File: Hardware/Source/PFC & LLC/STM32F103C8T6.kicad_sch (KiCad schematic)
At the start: 107 parts, among them J3 Conn_01x06_Socket, J4 Conn_01x02_Socket, J5 Conn_01x04_Pin, J6 Conn_01x05_Socket, Q6 LN2302LT1G, Q7 LN2302LT1G, Q8 LN2302LT1G, Q9 MMBT2222A, SW1 SW_Push, U10 ADS1115IDGS, U11 STM32F103C8T6, U12 MAX485CSA, Y1 Crystal_8MHz_SMD-4PIN

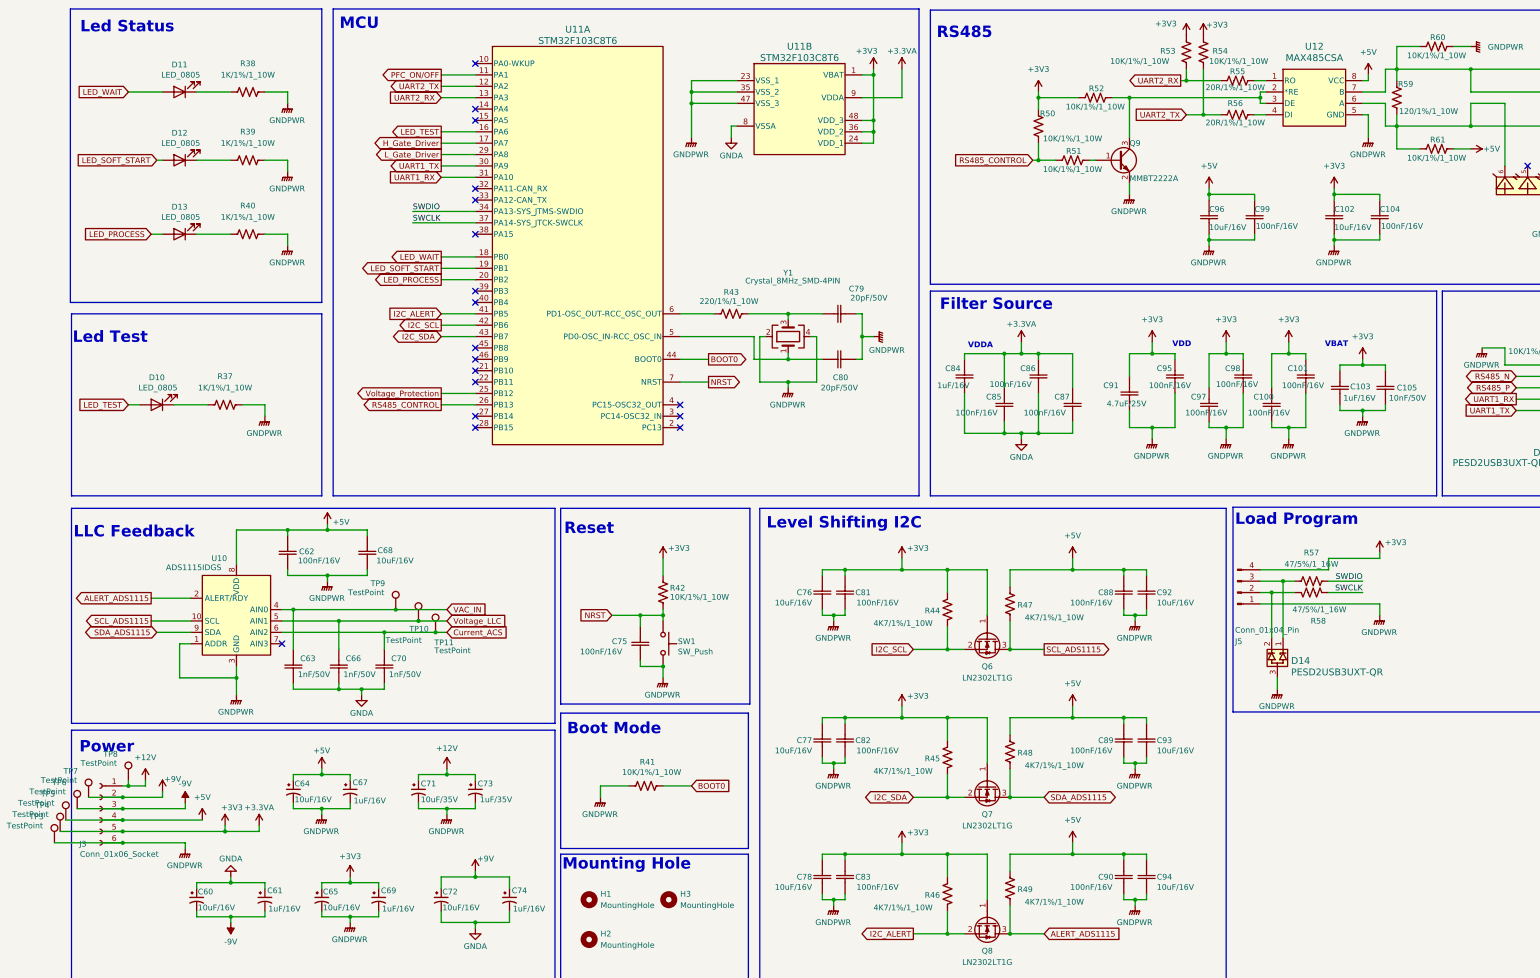
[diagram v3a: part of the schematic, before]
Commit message: Update PFC&LLC
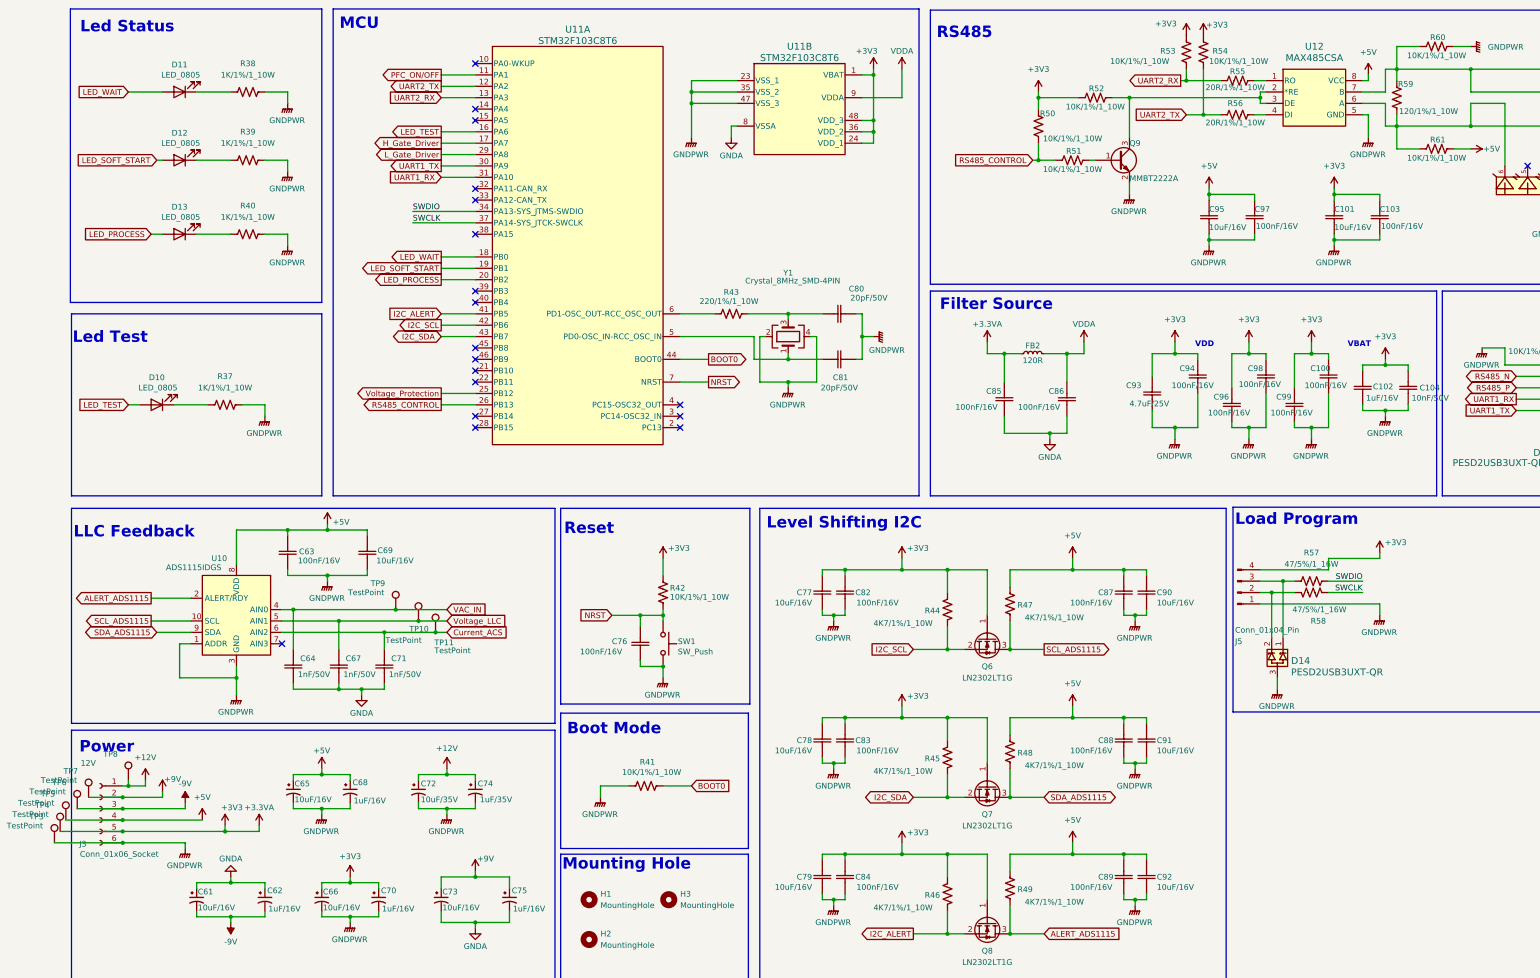
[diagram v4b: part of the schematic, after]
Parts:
- removed C84: 1uF/16V, charge_battery_footprint_lib:Ceramic_Cap_0603, symbol charge_battery_sym_lib:Ceramic_Cap_SMD_1uF_16V
- removed C87: 100nF/16V, charge_battery_footprint_lib:Ceramic_Cap_0603, symbol charge_battery_sym_lib:Ceramic_Cap_SMD_100nF_16V
- added FB2: 120R, Inductor_SMD:L_0805_2012Metric, symbol Device:L_Small
- TP8: value TestPoint -> 12V
- renumbered C101 to C100, C102 to C101, C103 to C102, C104 to C103, C105 to C104, C60 to C61, C61 to C62, C62 to C63, C63 to C64, C64 to C65, C65 to C66, C66 to C67, C67 to C68, C68 to C69, C69 to C70, C70 to C71, C71 to C72, C72 to C73, C73 to C74, C74 to C75, C75 to C76, C76 to C77, C77 to C78, C78 to C79, C79 to C80, C80 to C81, C81 to C82, C82 to C83, C83 to C84, C88 to C87, C89 to C88, C90 to C89, C92 to C90, C93 to C91, C94 to C92, C91 to C93, C95 to C94, C96 to C95, C97 to C96, C99 to C97, C100 to C99
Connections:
- net +3.3VA: now also FB2.1; no longer C86.2, U11.9 (VDDA)
- new net VDDA: C86.2, FB2.2, U11.9 (VDDA)
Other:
- note removed: "VDDA"
- moved on the sheet: C100, C102, C104, C85, C86, C93, C94, C96, C98, C99

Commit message: PFC&LLC almost done
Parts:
- TP3: value TestPoint -> GND
- TP4: value TestPoint -> 3V3
- TP5: value TestPoint -> 5V
- TP6: value TestPoint -> -9V
- TP7: value TestPoint -> 9V
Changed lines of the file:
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@@
 	)
 	(rectangle
-		(start 25.4 193.294)
+		(start 15.24 193.294)
 		(end 133.35 248.92)
 		(stroke
@@
 				)
 				(justify left)
+				(hide yes)
 			)
 		)
-		(property "Value" "TestPoint"
-			(at 10.922 214.63 0)
+		(property "Value" "GND"
+			(at 16.256 214.376 0)
 			(effects
 				(font
@@
 				)
 				(justify left)
+				(hide yes)
 			)
 		)
-		(property "Value" "TestPoint"
-			(at 18.542 204.47 0)
+		(property "Value" "9V"
+			(at 27.94 203.2 0)
 			(effects
 				(font
@@
 		(dnp no)
 		(property "Reference" "TP8"
-			(at 32.512 198.628 0)
+			(at 33.782 200.66 0)
 			(effects
 				(font
@@
 				)
 				(justify left)
+				(hide yes)
 			)
 		)
 		(property "Value" "12V"
-			(at 27.432 200.66 0)
+			(at 32.766 200.914 0)
 			(effects
 				(font
@@
 				)
 				(justify left)
+				(hide yes)
 			)
 		)
-		(property "Value" "TestPoint"
-			(at 12.192 212.09 0)
+		(property "Value" "3V3"
+			(at 18.796 210.82 0)
 			(effects
 				(font
@@
 				)
 				(justify left)
+				(hide yes)
 			)
 		)
-		(property "Value" "TestPoint"
-			(at 16.002 207.01 0)
+		(property "Value" "-9V"
+			(at 22.606 205.994 0)
 			(effects
 				(font
@@
 				)
 				(justify left)
+				(hide yes)
 			)
 		)
-		(property "Value" "TestPoint"
-			(at 13.462 209.55 0)
+		(property "Value" "5V"
+			(at 21.336 208.28 0)
 			(effects
 				(font

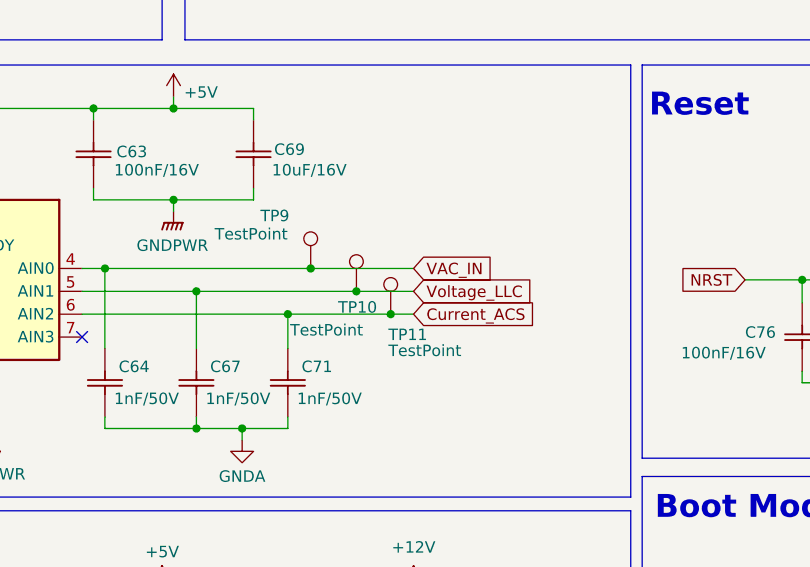
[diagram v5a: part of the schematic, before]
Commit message: Update PFC&LLC
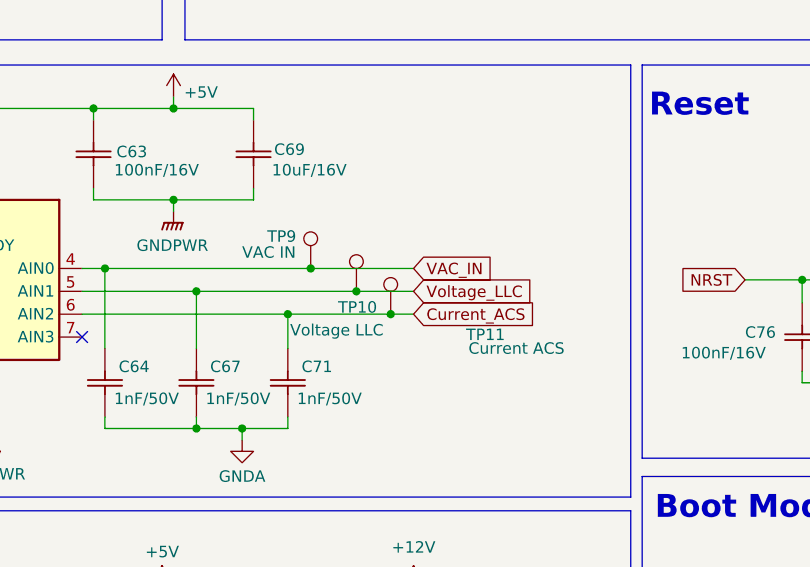
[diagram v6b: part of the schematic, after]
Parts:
- TP10: value TestPoint -> Voltage LLC; footprint TestPoint:TestPoint_Pad_D1.0mm -> TestPoint:TestPoint_Bridge_Pitch2.0mm_Drill0.7mm
- TP11: value TestPoint -> Current ACS; footprint TestPoint:TestPoint_Pad_D1.0mm -> TestPoint:TestPoint_Bridge_Pitch2.0mm_Drill0.7mm
- TP9: value TestPoint -> VAC IN; footprint TestPoint:TestPoint_Pad_D1.0mm -> TestPoint:TestPoint_Bridge_Pitch2.0mm_Drill0.7mm
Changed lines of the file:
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@@
 		(dnp no)
 		(property "Reference" "TP9"
-			(at 92.202 160.528 0)
+			(at 92.964 162.814 0)
 			(effects
 				(font
@@
 			)
 		)
-		(property "Value" "TestPoint"
-			(at 87.122 162.56 0)
+		(property "Value" "VAC IN"
+			(at 90.17 164.592 0)
 			(effects
 				(font
@@
 			)
 		)
-		(property "Footprint" "TestPoint:TestPoint_Pad_D1.0mm"
+		(property "Footprint" "TestPoint:TestPoint_Bridge_Pitch2.0mm_Drill0.7mm"
 			(at 102.87 166.37 0)
 			(effects
@@
 			)
 		)
-		(property "Value" "TestPoint"
+		(property "Value" "Voltage LLC"
 			(at 95.504 173.228 0)
 			(effects
@@
 			)
 		)
-		(property "Footprint" "TestPoint:TestPoint_Pad_D1.0mm"
+		(property "Footprint" "TestPoint:TestPoint_Bridge_Pitch2.0mm_Drill0.7mm"
 			(at 107.95 168.91 0)
 			(effects
@@
 		(dnp no)
 		(property "Reference" "TP11"
-			(at 106.426 173.736 0)
+			(at 115.062 173.736 0)
 			(effects
 				(font
@@
 			)
 		)
-		(property "Value" "TestPoint"
-			(at 106.426 175.514 0)
+		(property "Value" "Current ACS"
+			(at 115.316 175.26 0)
 			(effects
 				(font
@@
 			)
 		)
-		(property "Footprint" "TestPoint:TestPoint_Pad_D1.0mm"
+		(property "Footprint" "TestPoint:TestPoint_Bridge_Pitch2.0mm_Drill0.7mm"
 			(at 111.76 171.45 0)
 			(effects

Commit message: Update Lib PFC
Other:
- moved on the sheet: C61, C62, C65, C66, C68, C70, C72, C73, C74, C75, C76, C77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

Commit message: Exported BOM List 4 boards
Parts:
- J3, J4: Supply name (none) -> Thegioiic
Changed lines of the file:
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@@
+			)
+		)
+		(property "Supply name" "Thegioiic"
+			(at 33.02 212.09 0)
+			(effects
+				(font
+					(size 1.27 1.27)
+				)
+				(hide yes)
 			)
 		)
@@
 			(at 335.28 204.47 0)
 			(effects
+				(font
+					(size 1.27 1.27)
+				)
+				(hide yes)
+			)
+		)
+		(property "Supply name" "Thegioiic"
+			(at 335.28 204.47 0)
+			(effects
